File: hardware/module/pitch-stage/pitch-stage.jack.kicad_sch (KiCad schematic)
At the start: 1 part

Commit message: WIP module schematics: footprints, bought-part fields, and the two board projects (module-main, module-jack)
Recovered from a container restart; not yet exported or checked.

Co-Authored-By: Claude Opus 5.5 <noreply@anthropic.com>
Claude-Session: https://claude.ai/code/session_01LmB4muFXnoLprWX4JzuJ5A
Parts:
- J-CV-PITCH: footprint (none) -> Connector_Audio:Jack_3.5mm_QingPu_WQP-PJ398SM_Vertical_CircularHoles; Assembly (none) -> hand; MPN (none) -> PJ398SM; Manufacturer (none) -> Thonk
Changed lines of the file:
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@@
     (property "Reference" "J-CV-PITCH" (at 43.18 49.53 0) (effects (font (size 1.27 1.27)) (justify left)))
     (property "Value" "PJ398SM" (at 43.18 52.07 0) (effects (font (size 1.27 1.27)) (justify left)))
-    (property "Footprint" "" (at 40.64 50.8 0) (effects (font (size 1.27 1.27)) hide))
+    (property "Footprint" "Connector_Audio:Jack_3.5mm_QingPu_WQP-PJ398SM_Vertical_CircularHoles" (at 40.64 50.8 0) (effects (font (size 1.27 1.27)) hide))
     (property "Datasheet" "" (at 40.64 50.8 0) (effects (font (size 1.27 1.27)) hide))
     (property "Row" "J-CV" (at 40.64 50.8 0) (effects (font (size 1.27 1.27)) hide))
@@
     (property "Note" "THE JACK IS THIS CIRCUIT'S PART. module/panel owns the 6 mm hole and says the net is ours. Its third pin, the normalling switch contact, is unused and not netted" (at 40.64 50.8 0) (effects (font (size 1.27 1.27)) hide))
     (property "Pins_source" "datasheets/connectors/PJ398SM.kicad_mod pad names T, TN, S; datasheets/connectors/PJ398SM-drawing.jpg: 3 tip, 2 normalling contact, 1 sleeve. TN is not on this symbol: unused, not netted" (at 40.64 50.8 0) (effects (font (size 1.27 1.27)) hide))
+    (property "Manufacturer" "Thonk" (at 40.64 50.8 0) (effects (font (size 1.27 1.27)) hide))
+    (property "MPN" "PJ398SM" (at 40.64 50.8 0) (effects (font (size 1.27 1.27)) hide))
+    (property "LCSC" "" (at 40.64 50.8 0) (effects (font (size 1.27 1.27)) hide))
+    (property "Assembly" "hand" (at 40.64 50.8 0) (effects (font (size 1.27 1.27)) hide))
     (pin "S")
     (pin "T")
-    (instances (project "pitch-stage.jack" (path "/777e1e5e-b5e8-55e6-8f24-0d55726d01d7" (reference "J-CV-PITCH") (unit 1))) (project "pitch-stage" (path "/818bd2a7-cdf3-5daa-834c-14911dcdaa31/3ca85165-8ff2-5b92-af7f-5128b21a9b40" (reference "J-CV-PITCH") (unit 1))))
+    (instances (project "module-jack" (path "/f69c67ba-c380-5393-90d5-6d2847e300fb/deb60ac7-2399-5c17-a8b9-cc8927c73157" (reference "J1") (unit 1))) (project "pitch-stage.jack" (path "/777e1e5e-b5e8-55e6-8f24-0d55726d01d7" (reference "J-CV-PITCH") (unit 1))) (project "pitch-stage" (path "/818bd2a7-cdf3-5daa-834c-14911dcdaa31/3ca85165-8ff2-5b92-af7f-5128b21a9b40" (reference "J-CV-PITCH") (unit 1))))
   )
   (wire (pts (xy 45.72 50.8) (xy 48.26 50.8)) (stroke (width 0) (type default)))

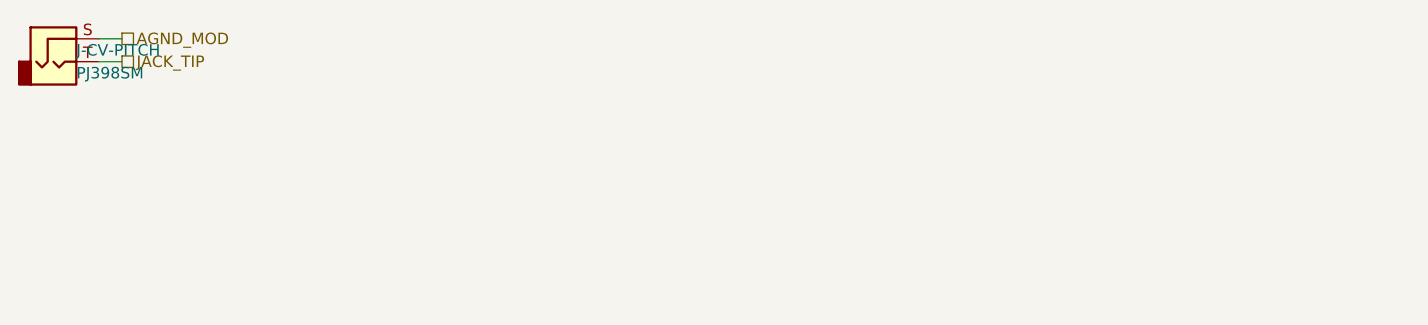
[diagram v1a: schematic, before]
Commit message: Pitch jack: D-ESD-PITCH, a bidirectional clamp at the jack ahead of the LT5400 (A2-2)
PESD15VL1BA tip to sleeve on the module jack board's page of pitch-stage,
so a strike is clamped before it crosses J-B2B-MOD. Datasheet banked in a
new fragment; BOM row, exports and renders regenerated.

Co-Authored-By: Claude Opus 5.5 <noreply@anthropic.com>
Claude-Session: https://claude.ai/code/session_01LmB4muFXnoLprWX4JzuJ5A
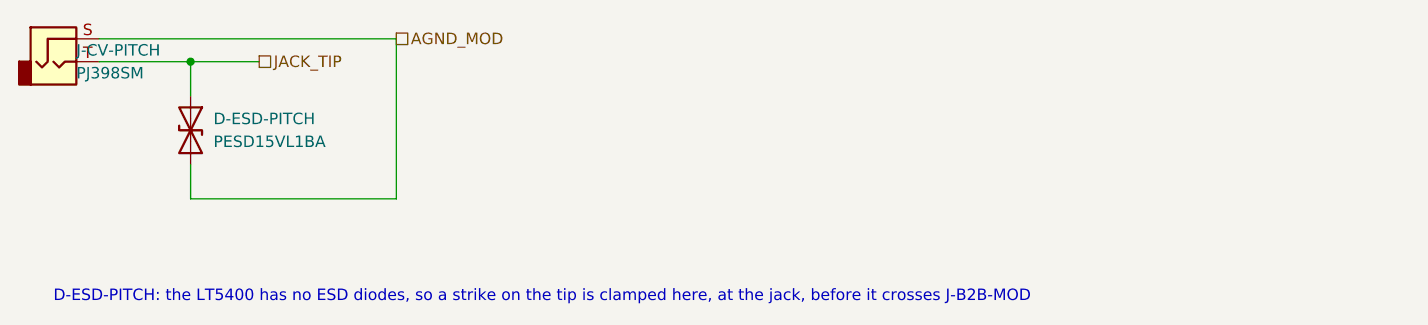
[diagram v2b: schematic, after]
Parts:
- added D-ESD-PITCH: PESD15VL1BA, Diode_SMD:D_SOD-323, symbol Device:D_TVS
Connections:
- net AGND_MOD: now also D-ESD-PITCH.2 (A2)
- net JACK_TIP: now also D-ESD-PITCH.1 (A1)
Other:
- note added: "D-ESD-PITCH: the LT5400 has no ESD diodes, so a strike on the tip is clamped here, at the jack, before it crosses J-B2B-MOD"
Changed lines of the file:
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@@
     (instances (project "module-jack" (path "/f69c67ba-c380-5393-90d5-6d2847e300fb/deb60ac7-2399-5c17-a8b9-cc8927c73157" (reference "J1") (unit 1))) (project "pitch-stage.jack" (path "/777e1e5e-b5e8-55e6-8f24-0d55726d01d7" (reference "J-CV-PITCH") (unit 1))) (project "pitch-stage" (path "/818bd2a7-cdf3-5daa-834c-14911dcdaa31/3ca85165-8ff2-5b92-af7f-5128b21a9b40" (reference "J-CV-PITCH") (unit 1))))
   )
-  (wire (pts (xy 45.72 50.8) (xy 48.26 50.8)) (stroke (width 0) (type default)))
-  (hierarchical_label "JACK_TIP" (shape passive) (at 48.26 50.8 0) (effects (font (size 1.27 1.27)) (justify left))
-    (property "Dir" "ref" (at 48.26 50.8 0) (effects (font (size 1.27 1.27)) hide)))
-  (wire (pts (xy 45.72 48.26) (xy 48.26 48.26)) (stroke (width 0) (type default)))
-  (hierarchical_label "AGND_MOD" (shape passive) (at 48.26 48.26 0) (effects (font (size 1.27 1.27)) (justify left))
-    (property "Dir" "ref" (at 48.26 48.26 0) (effects (font (size 1.27 1.27)) hide))
-    (property "From" "module/power-entry" (at 48.26 48.26 0) (effects (font (size 1.27 1.27)) hide))
-    (property "Figure" "dig-gnd-topology" (at 48.26 48.26 0) (effects (font (size 1.27 1.27)) hide)))
+  (wire (pts (xy 45.72 50.8) (xy 55.88 50.8)) (stroke (width 0) (type default)))
+  (hierarchical_label "JACK_TIP" (shape passive) (at 63.5 50.8 0) (effects (font (size 1.27 1.27)) (justify left))
+    (property "Dir" "ref" (at 63.5 50.8 0) (effects (font (size 1.27 1.27)) hide)))
+  (wire (pts (xy 45.72 48.26) (xy 78.74 48.26)) (stroke (width 0) (type default)))
+  (hierarchical_label "AGND_MOD" (shape passive) (at 78.74 48.26 0) (effects (font (size 1.27 1.27)) (justify left))
+    (property "Dir" "ref" (at 78.74 48.26 0) (effects (font (size 1.27 1.27)) hide))
+    (property "From" "module/power-entry" (at 78.74 48.26 0) (effects (font (size 1.27 1.27)) hide))
+    (property "Figure" "dig-gnd-topology" (at 78.74 48.26 0) (effects (font (size 1.27 1.27)) hide)))
+  (symbol (lib_id "Device:D_TVS") (at 55.88 58.42 270) (unit 1)
+    (in_bom yes) (on_board yes) (dnp no)
+    (property "Reference" "D-ESD-PITCH" (at 58.42 57.15 270) (effects (font (size 1.27 1.27)) (justify right)))
+    (property "Value" "PESD15VL1BA" (at 58.42 59.69 270) (effects (font (size 1.27 1.27)) (justify right)))
+    (property "Footprint" "Diode_SMD:D_SOD-323" (at 55.88 58.42 0) (effects (font (size 1.27 1.27)) hide))
+    (property "Datasheet" "" (at 55.88 58.42 0) (effects (font (size 1.27 1.27)) hide))
+    (property "Row" "D-ESD-PITCH" (at 55.88 58.42 0) (effects (font (size 1.27 1.27)) hide))
+    (property "Pins" "K1=1(A1) K2=2(A2)" (at 55.88 58.42 0) (effects (font (size 1.27 1.27)) hide))
+    (property "Note" "JACK-SIDE ESD CLAMP for the LT5400 (owner, 2026-10-01). Bidirectional, tip to sleeve, AT THE JACK on this board, so a strike on the tip is clamped before it crosses J-B2B-MOD and reaches TRIM-GAIN and RN-PITCH, which has no internal ESD diodes (LT5400.pdf p.6; its Figure 1 second option, a bidirectional zener to ground at the connector). On the DC feedback node, so its leakage and capacitance sit inside the loop: no accuracy cost (pitch-stage.md, The jack-side ESD clamp)" (at 55.88 58.42 0) (effects (font (size 1.27 1.27)) hide))
+    (property "Pins_source" "datasheets/discrete-and-power/NEXPERIA-PESD15VL1BA.pdf Table 2 pinning: 1 K1 cathode (diode 1), 2 K2 cathode (diode 2); bidirectional and symmetric, so either way round" (at 55.88 58.42 0) (effects (font (size 1.27 1.27)) hide))
+    (property "Manufacturer" "Nexperia" (at 55.88 58.42 0) (effects (font (size 1.27 1.27)) hide))
+    (property "MPN" "PESD15VL1BA,115" (at 55.88 58.42 0) (effects (font (size 1.27 1.27)) hide))
+    (property "LCSC" "C85378" (at 55.88 58.42 0) (effects (font (size 1.27 1.27)) hide))
+    (property "Assembly" "machine" (at 55.88 58.42 0) (effects (font (size 1.27 1.27)) hide))
+    (pin "1")
+    (pin "2")
+    (instances (project "module-jack" (path "/f69c67ba-c380-5393-90d5-6d2847e300fb/deb60ac7-2399-5c17-a8b9-cc8927c73157" (reference "D2") (unit 1))) (project "pitch-stage.jack" (path "/777e1e5e-b5e8-55e6-8f24-0d55726d01d7" (reference "D-ESD-PITCH") (unit 1))) (project "pitch-stage" (path "/818bd2a7-cdf3-5daa-834c-14911dcdaa31/3ca85165-8ff2-5b92-af7f-5128b21a9b40" (reference "D-ESD-PITCH") (unit 1))))
+  )
+  (wire (pts (xy 55.88 50.8) (xy 63.5 50.8)) (stroke (width 0) (type default)))
+  (wire (pts (xy 55.88 50.8) (xy 55.88 54.61)) (stroke (width 0) (type default)))
+  (wire (pts (xy 55.88 62.23) (xy 55.88 66.04)) (stroke (width 0) (type default)))
+  (wire (pts (xy 55.88 66.04) (xy 78.74 66.04)) (stroke (width 0) (type default)))
+  (wire (pts (xy 78.74 66.04) (xy 78.74 48.26)) (stroke (width 0) (type default)))
+  (junction (at 55.88 50.8) (diameter 0) (color 0 0 0 0))
+  (text "D-ESD-PITCH: the LT5400 has no ESD diodes, so a strike on the tip is clamped here, at the jack, before it crosses J-B2B-MOD" (at 40.64 76.2 0) (effects (font (size 1.27 1.27)) (justify left top)))
   (sheet_instances (path "/" (page "1")))
 )
